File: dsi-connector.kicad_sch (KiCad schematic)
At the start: 13 parts, among them J1 Plug_Molex_SlimStack_2x20_556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

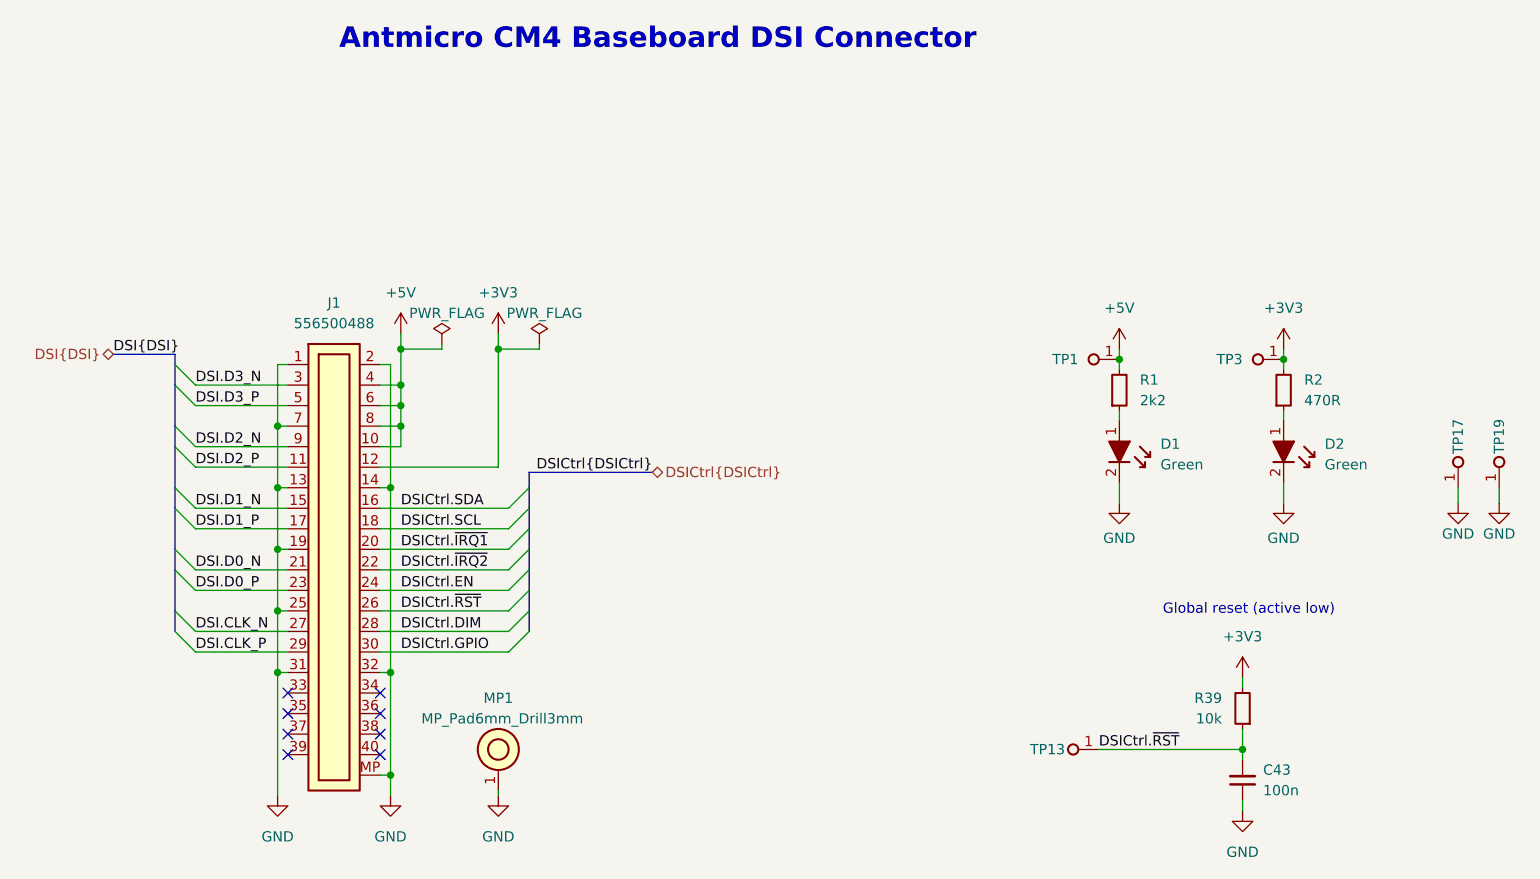
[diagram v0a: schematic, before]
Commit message: [#58170] Clean ERC (update from lib; align to grid)
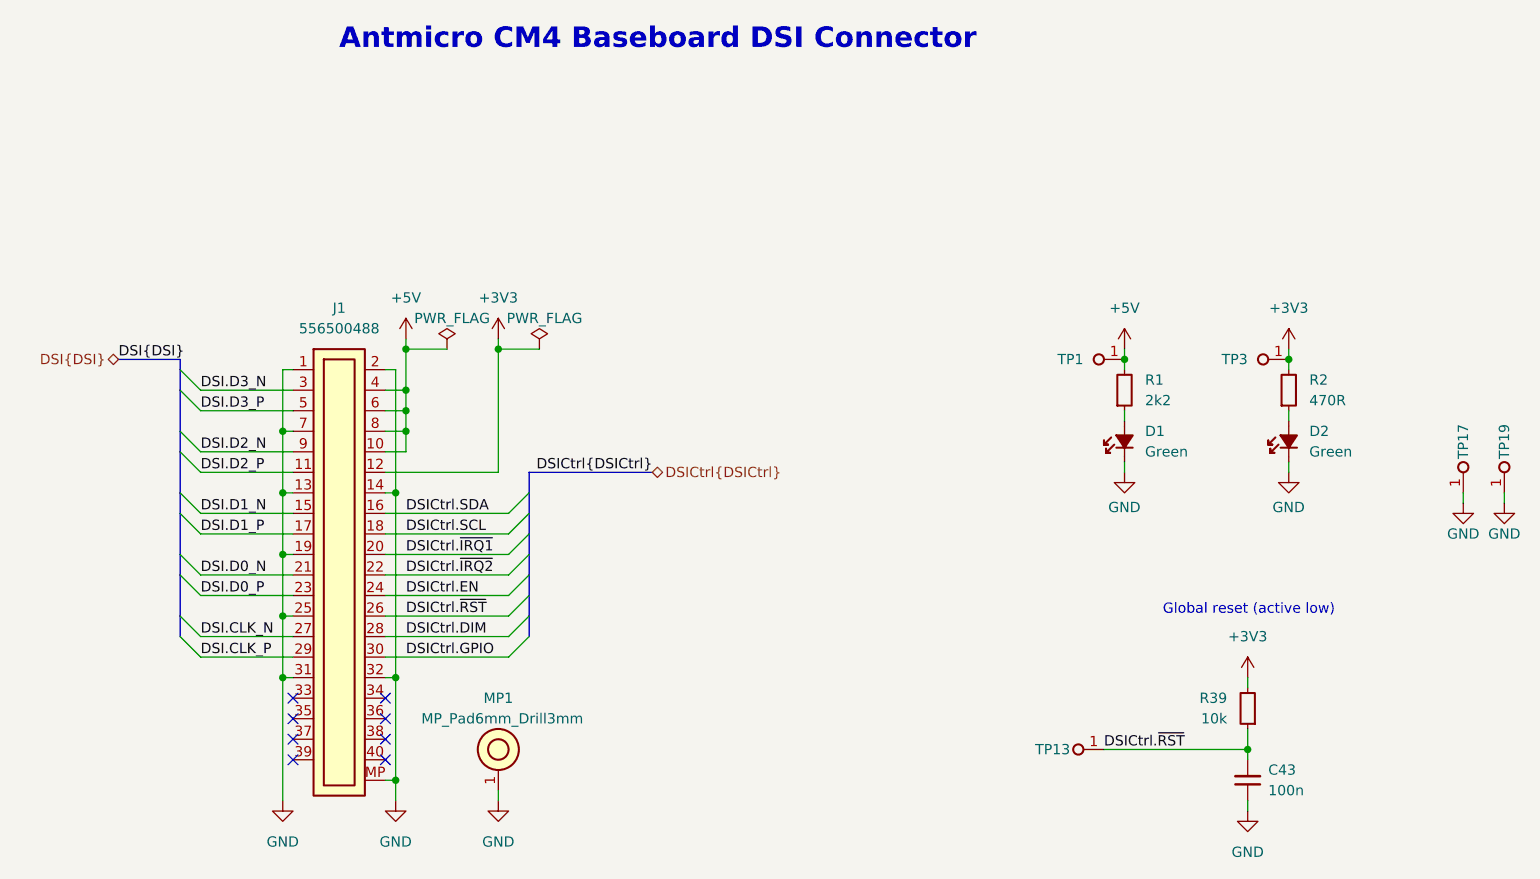
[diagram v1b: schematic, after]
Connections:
- net GND: now also D1.1 (C), D2.1 (C); no longer D1.2, D2.2
- net at R2.1: now also D2.2 (A); no longer D2.1
- net at R1.1: now also D1.2 (A); no longer D1.1
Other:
- moved on the sheet: C43, J1, R1, R2, R39, TP1, TP13, TP17, TP19, TP3

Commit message: [#61475] Update symbols from library & resolve ERC issues
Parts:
- C43, D1, D2, MP1, R1, R2, R39, TP1, TP13, TP17, TP19, TP3: Public (none) -> False
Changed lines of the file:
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@@
       (effects (font (size 1.27 1.27)) hide)
+    )
+    (property "Public" "False" (at 217.17 46.99 0)
+      (effects (font (size 1.27 1.27)) (justify left bottom) hide)
     )
     (pin "1")
@@
       (effects (font (size 1.27 1.27)) (justify left bottom) hide)
     )
+    (property "Public" "False" (at 191.77 86.36 0)
+      (effects (font (size 1.27 1.27)) (justify left bottom) hide)
+    )
     (pin "1")
     (pin "2")
@@
       (effects (font (size 1.27 1.27)) (justify left bottom) hide)
     )
+    (property "Public" "False" (at 255.27 95.25 0)
+      (effects (font (size 1.27 1.27)) (justify left bottom) hide)
+    )
     (pin "1")
     (pin "2")
@@
       (effects (font (size 1.27 1.27)) (justify left bottom) hide)
     )
+    (property "Public" "False" (at 257.81 46.99 0)
+      (effects (font (size 1.27 1.27)) (justify left bottom) hide)
+    )
     (pin "1")
     (pin "2")
@@
       (effects (font (size 1.27 1.27)) (justify left bottom) hide)
     )
+    (property "Public" "False" (at 237.49 46.99 0)
+      (effects (font (size 1.27 1.27)) (justify left bottom) hide)
+    )
     (pin "1")
     (pin "2")
@@
     (property "Color" "Green" (at 229.87 72.39 90)
       (effects (font (size 1.27 1.27)) (justify right))
+    )
+    (property "Public" "False" (at 245.11 53.34 0)
+      (effects (font (size 1.27 1.27)) (justify left bottom) hide)
     )
     (pin "1")
@@
       (effects (font (size 1.27 1.27) (thickness 0.15)) (justify left bottom) hide)
     )
+    (property "Public" "False" (at 267.97 67.31 0)
+      (effects (font (size 1.27 1.27)) (justify left bottom) hide)
+    )
     (pin "1")
     (instances
@@
       (effects (font (size 1.27 1.27) (thickness 0.15)) (justify left bottom) hide)
     )
+    (property "Public" "False" (at 262.89 67.31 0)
+      (effects (font (size 1.27 1.27)) (justify left bottom) hide)
+    )
     (pin "1")
     (instances
@@
       (effects (font (size 1.27 1.27) (thickness 0.15)) (justify left bottom) hide)
     )
+    (property "Public" "False" (at 144.78 93.98 0)
+      (effects (font (size 1.27 1.27)) (justify left bottom) hide)
+    )
     (pin "1")
     (instances
@@
     (property "Color" "Green" (at 209.55 72.39 90)
       (effects (font (size 1.27 1.27)) (justify right))
+    )
+    (property "Public" "False" (at 224.79 53.34 0)
+      (effects (font (size 1.27 1.27)) (justify left bottom) hide)
     )
     (pin "1")
@@
       (effects (font (size 1.27 1.27)) hide)
     )
+    (property "Public" "False" (at 196.85 46.99 0)
+      (effects (font (size 1.27 1.27)) (justify left bottom) hide)
+    )
     (pin "1")
     (instances
@@
       (effects (font (size 1.27 1.27) (thickness 0.15)) (justify left bottom) hide)
     )
-    (pin "1")
+    (property "Public" "False" (at 194.31 95.25 0)
+      (effects (font (size 1.27 1.27)) (justify left bottom) hide)
+    )
+    (pin "1")
